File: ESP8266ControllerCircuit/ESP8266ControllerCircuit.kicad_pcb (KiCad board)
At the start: 2 copper layers, 75 x 30 mm, 25 parts, among them J1 Input, J2 Input, J3 Input, J4 Input, J5 Optional, U1 WeMos_mini, U2 EL3H7(B)(TA)-G, U3 PCF8574T/3,518

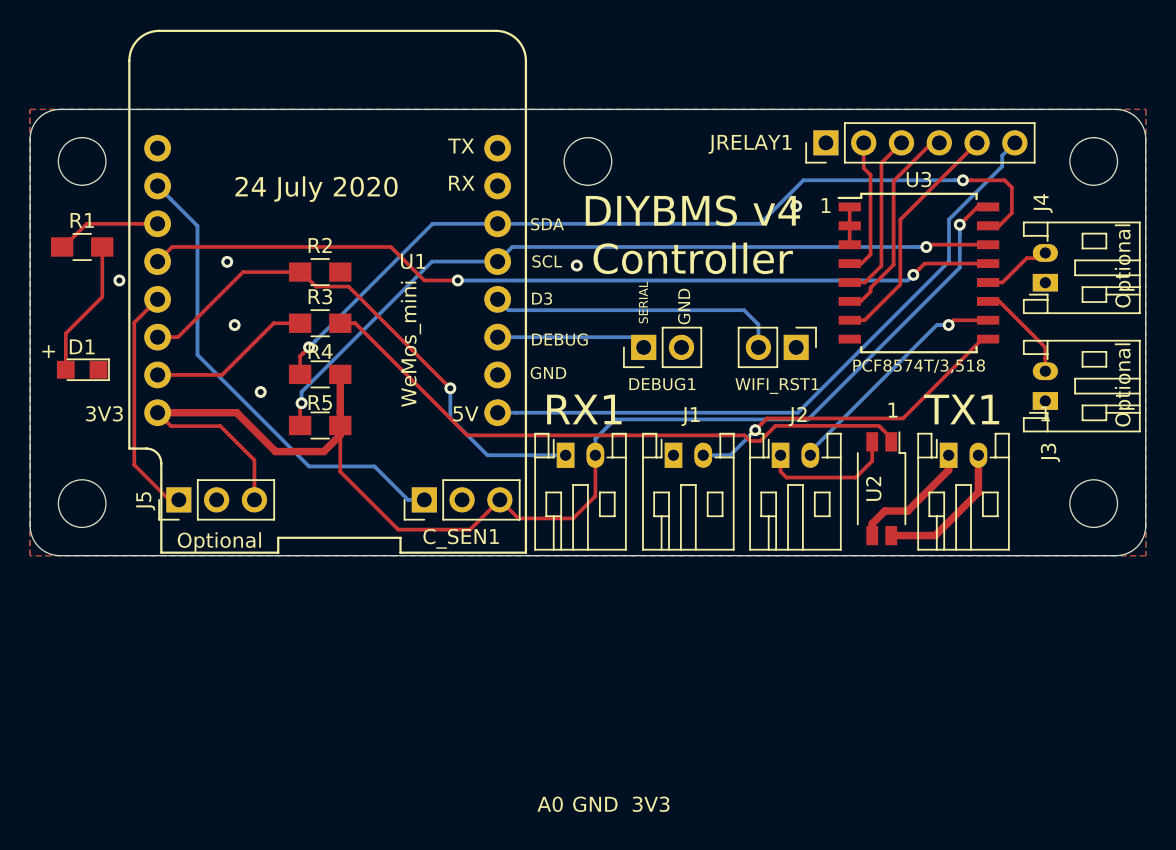
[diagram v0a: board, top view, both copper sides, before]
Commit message: More kicad6 migration
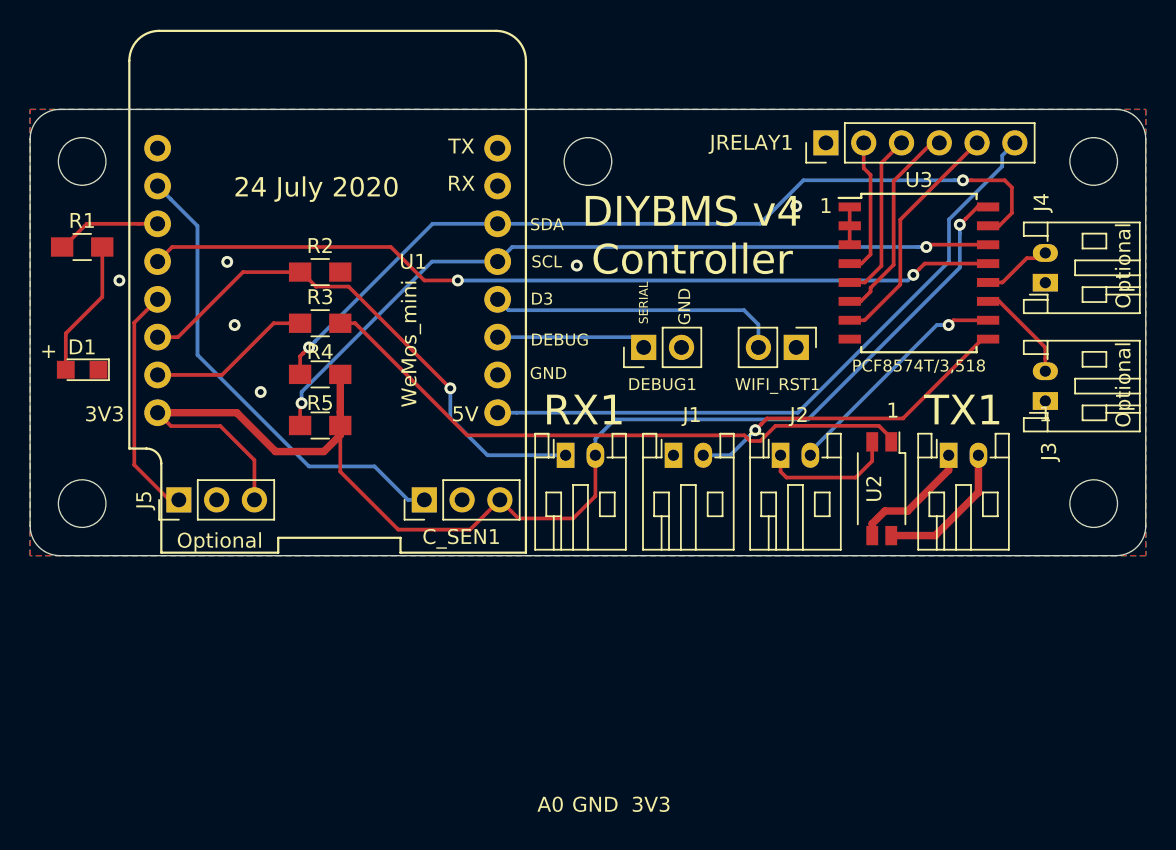
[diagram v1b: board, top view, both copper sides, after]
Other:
- net class Default removed
